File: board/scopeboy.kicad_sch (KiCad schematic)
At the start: 94 parts, among them J1 USB_C_Receptacle_USB2.0_16P, J2 SM03B-SRSS-TB, J3 SM03B-SRSS-TB, J4 Conn_01x10, J5 SM04B-SRSS-TB, J6 HDMI_A, SW1 SW_Push, SW2 SW_Push, SW3 RotaryEncoder_Switch, U1 W25Q128JVS, U2 DNF, U3 NCP1117-3.3_SOT223, U4 RP2350_80QFN, U5 LP2985-3.3, U6 LM27762, U7 ADC08060, Y1 ABM8-272-T3

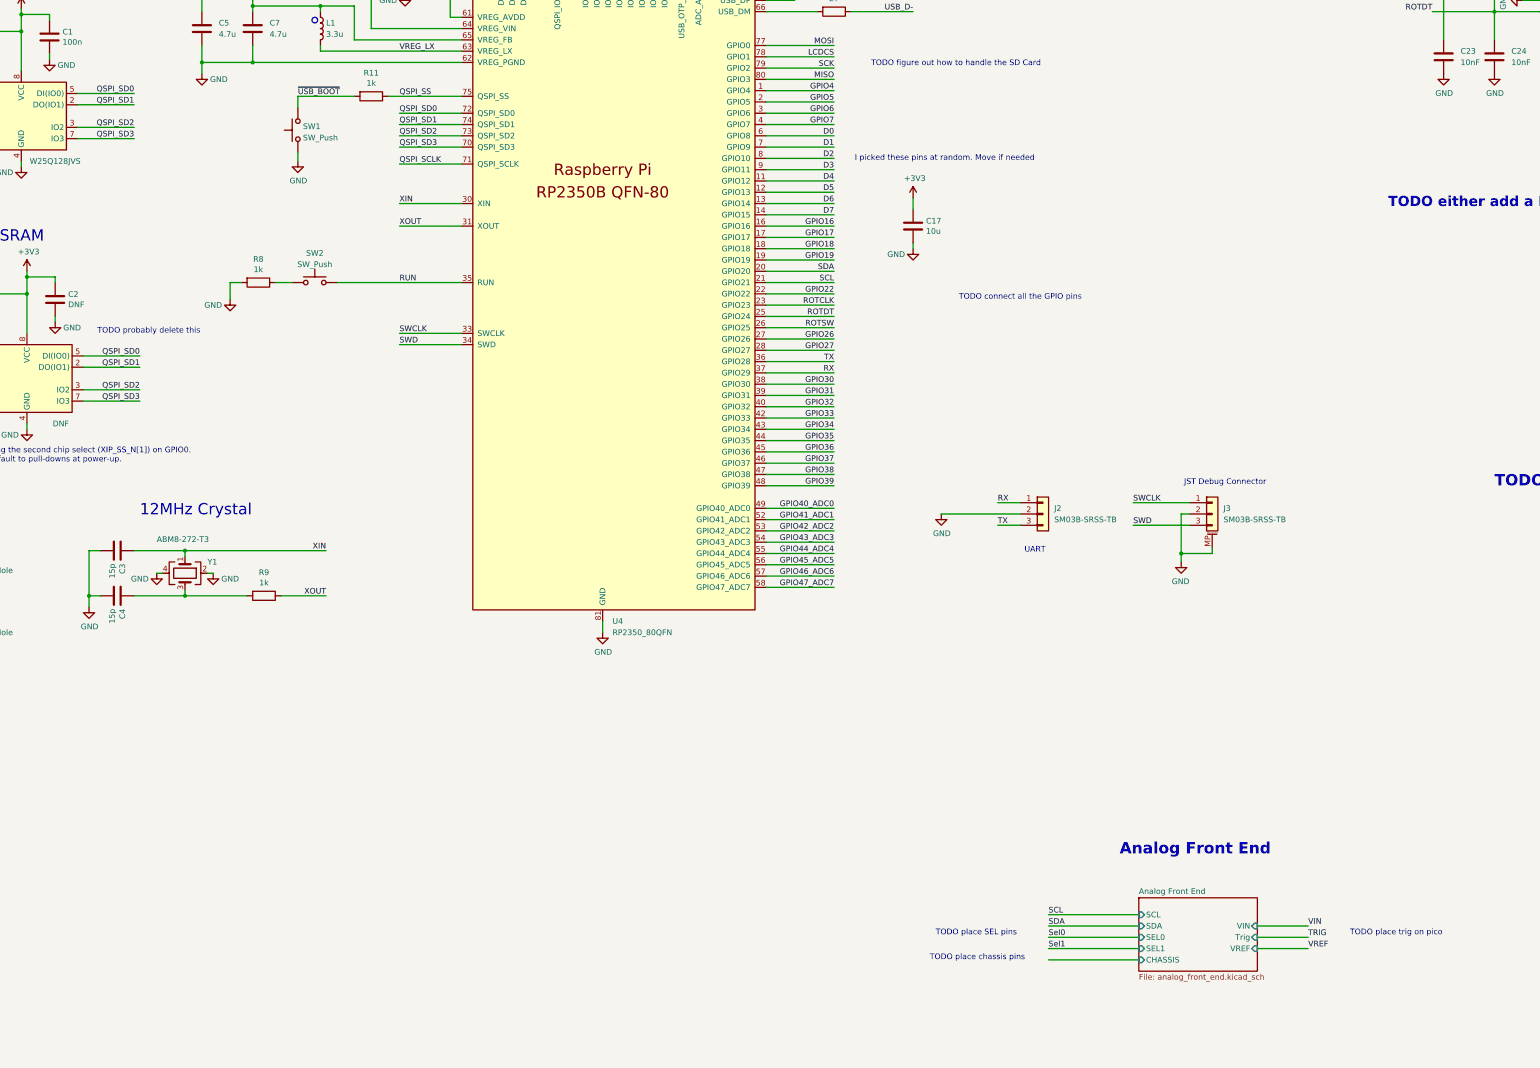
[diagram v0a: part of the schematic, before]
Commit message: Updated trig, sel0, sel1 pins
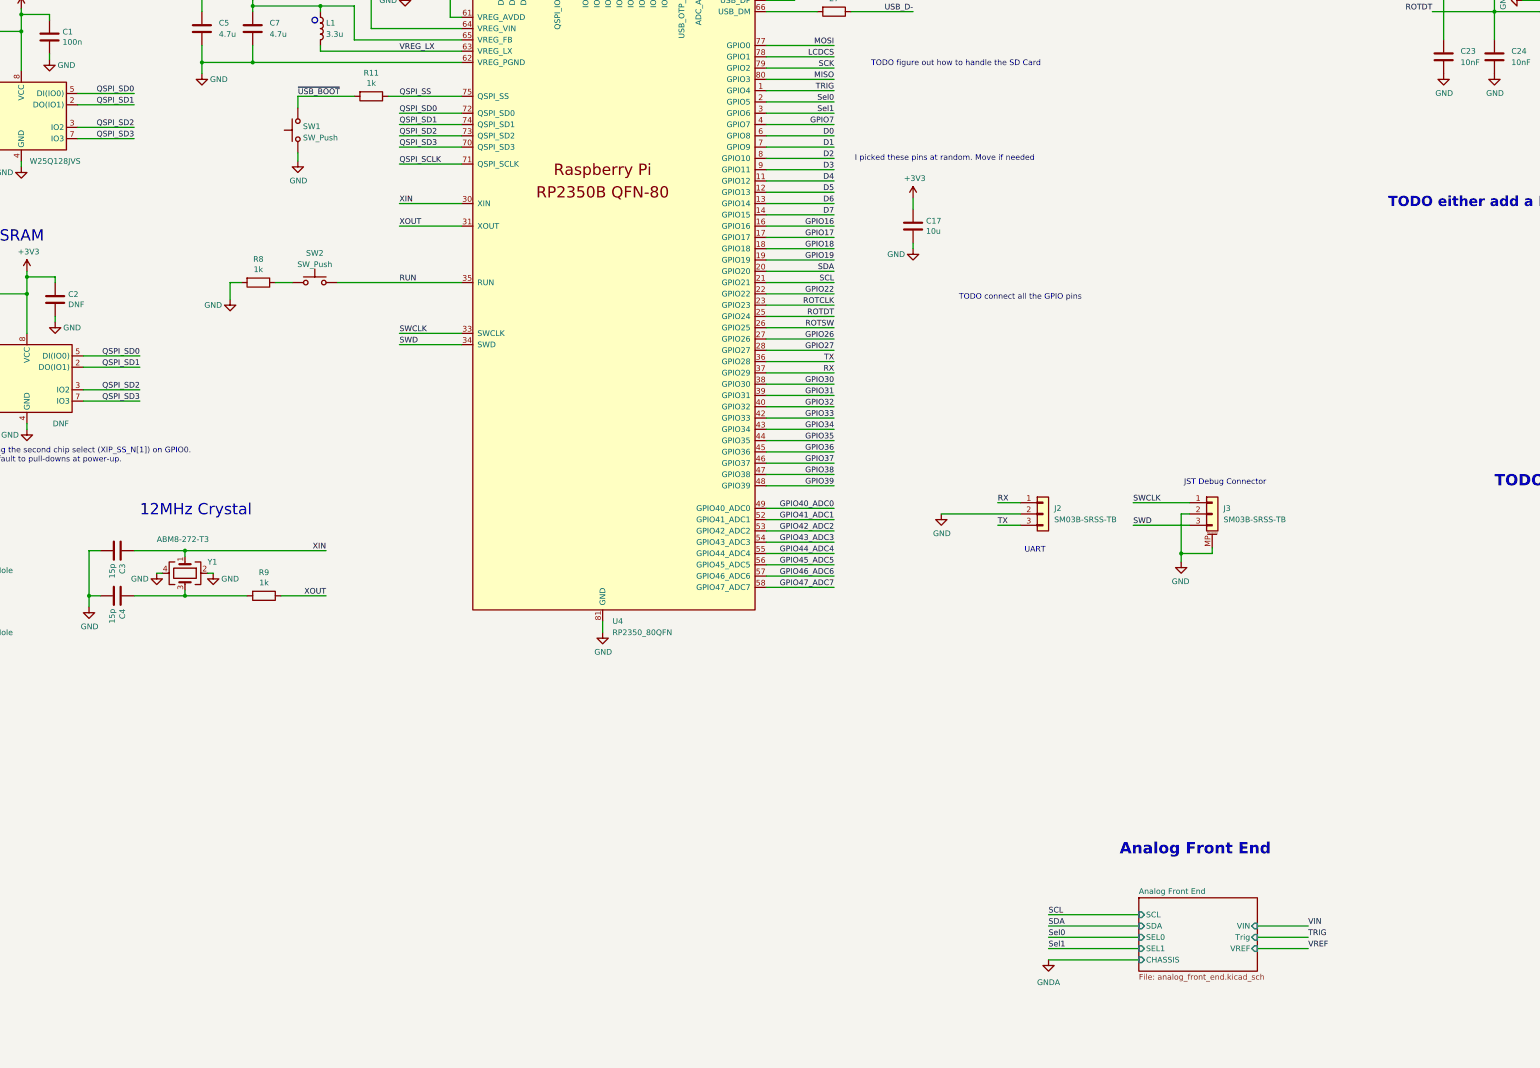
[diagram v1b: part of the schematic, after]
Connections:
- net GPIO4 is gone; now on net TRIG: U4.1 (GPIO4)
- net GPIO5 is gone; now on net Sel0: U4.2 (GPIO5)
- net GPIO6 is gone; now on net Sel1: U4.3 (GPIO6)
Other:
- note removed: "TODO place SEL pins"
- note removed: "TODO place chassis pins"
- note removed: "TODO place trig on pico"
- note removed: "TODO probably delete this"
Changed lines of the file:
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@@
 		)
 	)
-	(text "TODO place trig on pico"
-		(exclude_from_sim no)
-		(at 376.682 311.404 0)
-		(effects
-			(font
-				(size 1.27 1.27)
-			)
-		)
-	)
 	(text "12MHz Crystal"
 		(exclude_from_sim no)
@@
 		)
 	)
-	(text "TODO probably delete this"
-		(exclude_from_sim no)
-		(at 96.012 176.022 0)
-		(effects
-			(font
-				(size 1.27 1.27)
-			)
-		)
-	)
 	(text "Analog Front End"
 		(exclude_from_sim no)
@@
 		)
 	)
-	(text "TODO place SEL pins"
-		(exclude_from_sim no)
-		(at 282.194 311.404 0)
-		(effects
-			(font
-				(size 1.27 1.27)
-			)
-		)
-	)
 	(text "HDMI"
 		(exclude_from_sim no)
@@
 		)
 	)
-	(text "TODO place chassis pins"
-		(exclude_from_sim no)
-		(at 282.448 316.992 0)
-		(effects
-			(font
-				(size 1.27 1.27)
-			)
-		)
-	)
 	(junction
 		(at 52.07 60.96)
@@
 		)
 	)
+	(label "TRIG"
+		(at 250.19 121.92 180)
+		(effects
+			(font
+				(size 1.27 1.27)
+			)
+			(justify right bottom)
+		)
+	)
 	(label "SCL"
 		(at 250.19 165.1 180)
@@
 		)
 	)
+	(label "Sel0"
+		(at 250.19 124.46 180)
+		(effects
+			(font
+				(size 1.27 1.27)
+			)
+			(justify right bottom)
+		)
+	)
 	(label "SCK"
 		(at 250.19 116.84 180)
@@
 		)
 	)
+	(label "Sel1"
+		(at 250.19 127 180)
+		(effects
+			(font
+				(size 1.27 1.27)
+			)
+			(justify right bottom)
+		)
+	)
 	(label "GPIO36"
 		(at 250.19 203.2 180)
@@
 		)
 	)
-	(label "GPIO5"
-		(at 250.19 124.46 180)
-		(effects
-			(font
-				(size 1.27 1.27)
-			)
-			(justify right bottom)
-		)
-	)
 	(label "TX"
 		(at 287.02 219.71 0)
@@
 		)
 	)
-	(label "GPIO6"
-		(at 250.19 127 180)
-		(effects
-			(font
-				(size 1.27 1.27)
-			)
-			(justify right bottom)
-		)
-	)
 	(label "D1"
 		(at 250.19 134.62 180)
@@
 		)
 	)
-	(label "GPIO4"
-		(at 250.19 121.92 180)
-		(effects
-			(font
-				(size 1.27 1.27)
-			)
-			(justify right bottom)
-		)
-	)
 	(label "ROTSW"
 		(at 250.19 175.26 180)
@@
 					(unit 1)
 				)
+			)
+		)
+	)
+	(symbol
+		(lib_name "GNDA_1")
+		(lib_id "power:GNDA")
+		(at 298.45 317.5 0)
+		(unit 1)
+		(exclude_from_sim no)
+		(in_bom yes)
+		(on_board yes)
+		(dnp no)
+		(fields_autoplaced yes)
+		(property "Reference" "#PWR0143"
+			(at 298.45 323.85 0)
+			(effects
+				(font
+					(size 1.27 1.27)
+				)
+				(hide yes)
+			)
+		)
+		(property "Value" "GNDA"
+			(at 298.45 322.58 0)
+			(effects
+				(font
+					(size 1.27 1.27)
+				)
+			)
+		)
+		(property "Footprint" ""
+			(at 298.45 317.5 0)
+			(effects
+				(font
+					(size 1.27 1.27)
+				)
+				(hide yes)
+			)
+		)
+		(property "Datasheet" ""
+			(at 298.45 317.5 0)
+			(effects
+				(font
+					(size 1.27 1.27)
+				)
+				(hide yes)
+			)
+		)
+		(property "Description" "Power symbol creates a global label with name \"GNDA\" , analog ground"
+			(at 298.45 317.5 0)
+			(effects
+				(font
+					(size 1.27 1.27)
+				)
+				(hide yes)
+			)
+		)
+		(pin "1"
+		)
+		(instances
+			(project "scopeboy"
+				(path "/94683f5c-9cd9-448e-be96-9792537b5cb8"
+					(reference "#PWR0143")
+					(unit 1)
+				)

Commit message: Added battery JST connector
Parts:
- removed C29: 1u, Capacitor_SMD:C_0603_1608Metric, symbol Device:C
- removed C34: 10n, Capacitor_SMD:C_0603_1608Metric, symbol Device:C
- removed C37: 2.2u, Capacitor_SMD:C_0603_1608Metric, symbol Device:C
- removed U5: LP2985-3.3, Package_TO_SOT_SMD:SOT-23-5, symbol Regulator_Linear:LP2985-3.3
- added J8: Conn_01x02, Connector_JST:JST_PH_S2B-PH-SM4-TB_1x02-1MP_P2.00mm_Horizontal, symbol Connector_Generic:Conn_01x02
- U7: MFR. Part # (none) -> ADC08060CIMTX/NOPB; MRF. Part # ADC08060CIMTX/NOPB -> (none)
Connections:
- net VSYS is gone; now on net VBUS: C26.1, U6.12 (EN+), U6.3 (VIN), U6.8 (EN-)
- net GND: now also J8.2 (Pin_2)
- net VBUS: now also J8.1 (Pin_1)
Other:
- note added: "Battery Connector"
- note added: "TODO This should not connect directly to USB VBUS"
- note added: "TODO Update this to be a Buck Boost converter and add some way to handle both USB and Battery input"
- note removed: "PSU DIG."
- note removed: "TODO CHANGE THESE TO BATTERY VOLTAGES"
- note removed: "TODO either add a LiPo JST connector or a AA/AAA battery connector"
- note removed: "TODO this might need to be updated to work off of battery"
- note removed: "TODO this needs to be updated as well. I think I now have 2 digital power units with the analog side as well"

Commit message: Added power mux and USB protection
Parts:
- added C29: 10uF, Capacitor_SMD:C_1206_3216Metric, symbol Device:C
- added D6: SMBJ5.0A, Diode_SMD:D_SMB, symbol Device:D_Zener
- added F1: MINISMDC050F-2, Fuse:Fuse_1812_4532Metric, symbol Device:Polyfuse
- added R48: 100k, Resistor_SMD:R_0603_1608Metric, symbol Device:R
- added R49: 10K, Resistor_SMD:R_0603_1608Metric, symbol Device:R
- added R50: 47k, Resistor_SMD:R_0603_1608Metric, symbol Device:R
- added U5: TPS2116DRL, Package_TO_SOT_SMD:SOT-583-8, symbol Power_Management:TPS2116DRL
- R6, R7: MFR. Part # (none) -> CRCW12065K10FKEA; Manufacturer Part Number CRCW12065K10FKEA -> (none)
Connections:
- net GPIO32 is gone; now on net D0: U4.40 (GPIO32)
- net GPIO33 is gone; now on net D1: U4.42 (GPIO33)
- net GPIO34 is gone; now on net D2: U4.43 (GPIO34)
- net GPIO35 is gone; now on net D3: U4.44 (GPIO35)
- net GPIO36 is gone; now on net D4: U4.45 (GPIO36)
- net GPIO37 is gone; now on net D5: U4.46 (GPIO37)
- net GPIO38 is gone; now on net D6: U4.47 (GPIO38)
- net GPIO39 is gone; now on net D7: U4.48 (GPIO39)
- net +5V: no longer J6.18 (+5V), R19.1, R19.2
- net D0: no longer U4.6 (GPIO8)
- net D1: no longer U4.7 (GPIO9)
- net D2: no longer U4.8 (GPIO10)
- net D3: no longer U4.9 (GPIO11)
- net D4: no longer U4.11 (GPIO12)
- net D5: no longer U4.12 (GPIO13)
- net D6: no longer U4.13 (GPIO14)
- net D7: no longer U4.14 (GPIO15)
- net GND: now also J1.S1 (SHIELD), C29.1, D6.2 (A), R50.2, U5.1 (GND)
- net VBUS: now also J6.18 (+5V), R19.1, R19.2, C29.2, D6.1 (K), F1.2, R48.1, U5.3 (VIN1), U5.5 (MODE); no longer C6.1, J1.A4 (VBUS), J1.A9 (VBUS), J1.B4 (VBUS), J1.B9 (VBUS), J8.1 (Pin_1), U3.3 (VI)
- net GPIO12 renamed HDMI_D2P
- net HDMI_D2P: now also U4.11 (GPIO12)
- net GPIO13 renamed HDMI_D2N
- net HDMI_D2N: now also U4.12 (GPIO13)
- net GPIO14 renamed HDMI_CKP
- net HDMI_CKP: now also U4.13 (GPIO14)
- net GPIO15 renamed HDMI_CKN
- net HDMI_CKN: now also U4.14 (GPIO15)
- net GPIO16 renamed HDMI_D1P
- net GPIO17 renamed HDMI_D1N
- net GPIO18 renamed HDMI_D0P
- net GPIO19 renamed HDMI_D0N
- net GPIO7 renamed PowerStatus
- net PowerStatus: now also R49.1, U5.8 (ST)
- new net: F1.1, J1.A4 (VBUS), J1.A9 (VBUS), J1.B4 (VBUS), J1.B9 (VBUS)
- new net: R48.2, R50.1, U5.4 (PR1)
- new net VBat: J8.1 (Pin_1), U5.6 (VIN2)
- new net VDC: C6.1, R49.2, U3.3 (VI), U5.2 (VOUT), U5.7 (VOUT)
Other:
- note added: "HDMI use HSTX pins, they cannot be moved"
- note added: "I picked these pins (mostly) at random. Move if needed"
- note added: "Power Mux"
- note added: "TODO SD card should probably be on these pins since they are all SPI1"
- note added: "TODO Update this to be a Buck Boost converter"
- note added: "USB Protection"
- note added: "VBus is USB"
- note removed: "I picked these pins at random. Move if needed"
- note removed: "TODO This should not connect directly to USB VBUS"
- note removed: "TODO Update this to be a Buck Boost converter and add some way to handle both USB and Battery input"
- note removed: "TODO figure out how to handle the SD Card"
- moved on the sheet: C17, C6, C9, J8, U3

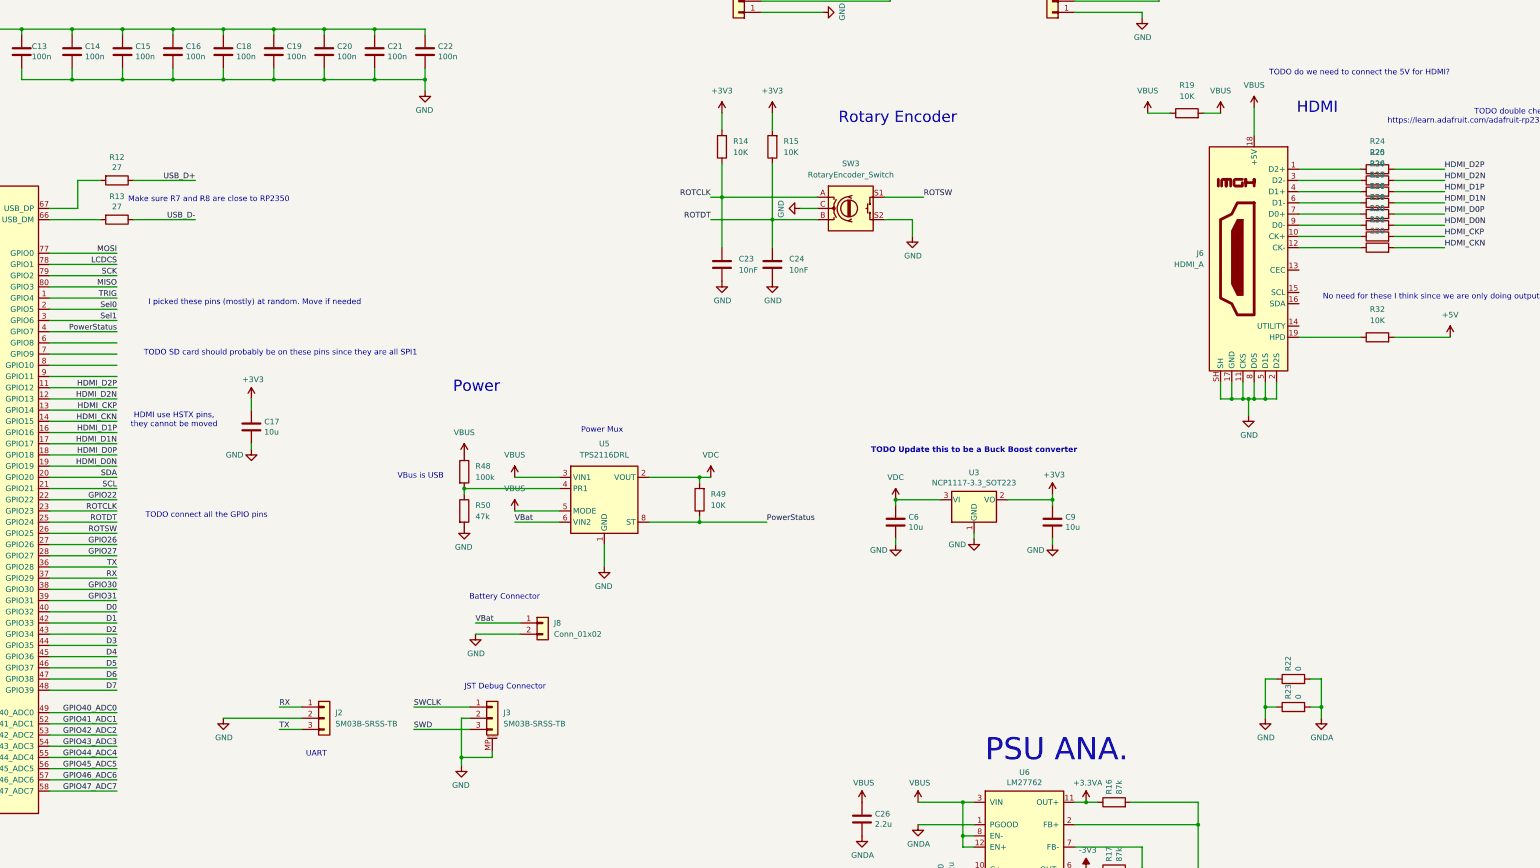
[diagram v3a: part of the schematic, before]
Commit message: Updated board with new power system
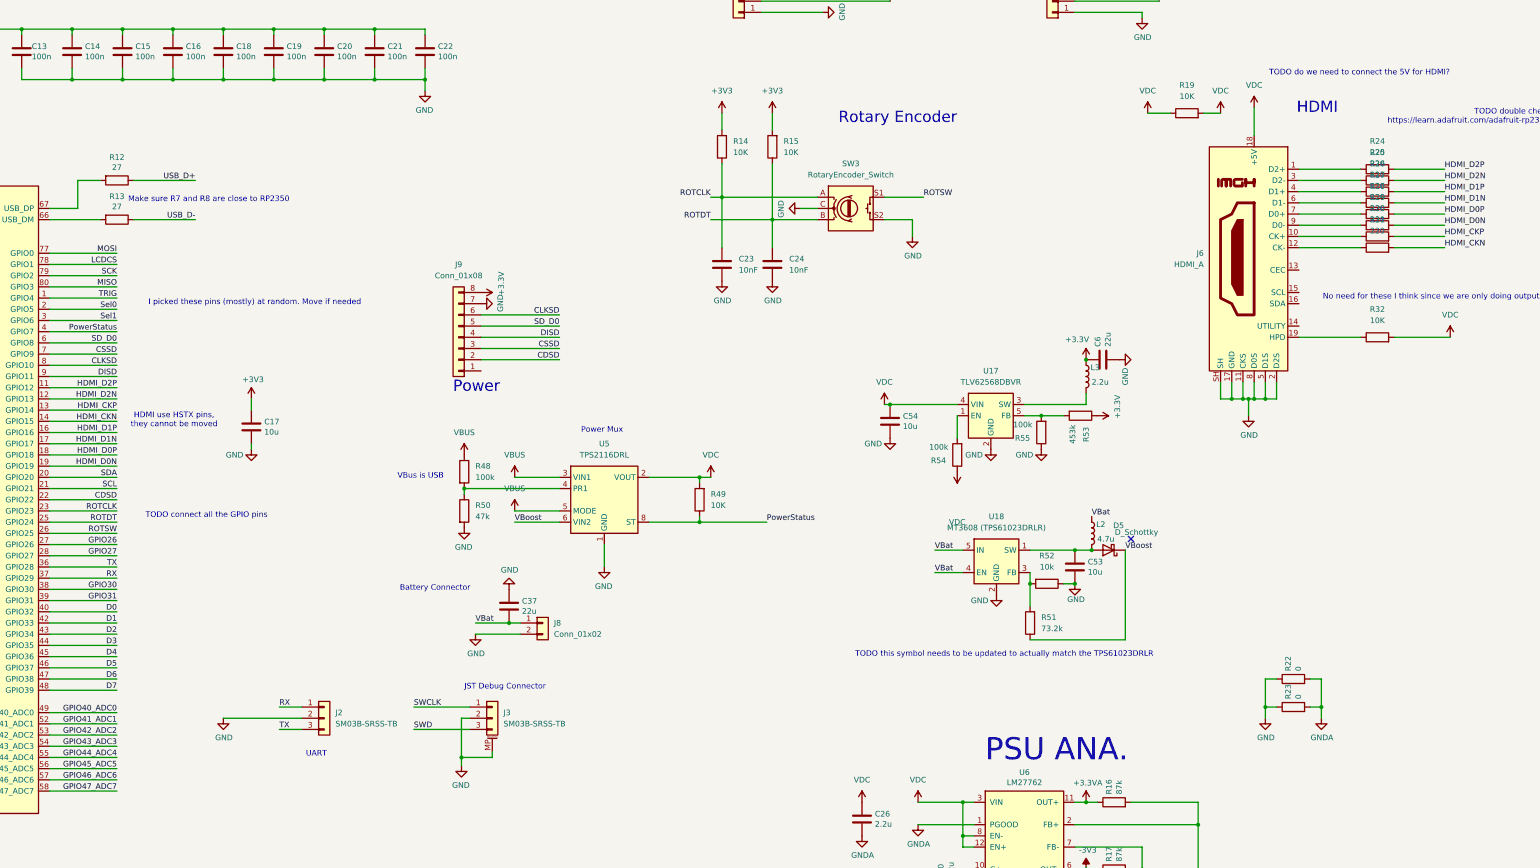
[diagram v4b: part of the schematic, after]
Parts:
- removed C9: 10u, Capacitor_SMD:C_0805_2012Metric, symbol Device:C
- removed U3: NCP1117-3.3_SOT223, Package_TO_SOT_SMD:SOT-223-3_TabPin2, symbol Regulator_Linear:NCP1117-3.3_SOT223
- added C37: 22u, Capacitor_SMD:C_0805_2012Metric, symbol Device:C
- added C53, C54: 10u, Capacitor_SMD:C_0805_2012Metric, symbol Device:C
- added D5: D_Schottky, Diode_SMD:D_SMA, symbol Device:D_Schottky
- added J9: Conn_01x08, Connector_PinHeader_2.54mm:PinHeader_1x08_P2.54mm_Vertical, symbol Connector_Generic:Conn_01x08
- added L2: 4.7u, Inductor_SMD:L_Bourns-SRN4018, symbol Device:L
- added L3: 2.2u, Inductor_SMD:L_Bourns-SRN4018, symbol Device:L
- added R51: 73.2k, Resistor_SMD:R_0603_1608Metric, symbol Device:R
- added R52: 10k, Resistor_SMD:R_0603_1608Metric, symbol Device:R
- added R53: 453k, Resistor_SMD:R_0603_1608Metric, symbol Device:R
- added R54, R55: 100k, Resistor_SMD:R_0603_1608Metric, symbol Device:R
- added U17: TLV62568DBVR, Package_TO_SOT_SMD:SOT-23-5, symbol Regulator_Switching:TLV62568DBV
- added U18: MT3608 (TPS61023DRLR), Package_TO_SOT_SMD:SOT-23-6, symbol Regulator_Switching:MT3608
- C6: value 10u -> 22u
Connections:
- net +5V is gone; now on net VDC: R32.2
- net GND: now also C37.1, C53.2, C54.2, J9.7 (Pin_7), R52.1, R55.1, U17.2 (GND), U18.2 (GND)
- net VBUS: no longer C26.1, J6.18 (+5V), R19.1, R19.2, U6.12 (EN+), U6.3 (VIN), U6.8 (EN-)
- net VBat: now also C37.2, L2.1, U18.4 (EN), U18.5 (IN); no longer U5.6 (VIN2)
- net VDC: now also C26.1, J6.18 (+5V), R19.1, R19.2, U6.12 (EN+), U6.3 (VIN), U6.8 (EN-), C54.1, R54.1, U17.4 (VIN); no longer C6.1
- net SD_D0: now reaches U4.6 (GPIO8)
- net SD_D0: now also J9.5 (Pin_5)
- net CSSD: now reaches U4.7 (GPIO9)
- net CSSD: now also J9.3 (Pin_3)
- net CLKSD: now reaches U4.8 (GPIO10)
- net CLKSD: now also J9.6 (Pin_6)
- net DISD: now reaches U4.9 (GPIO11)
- net DISD: now also J9.4 (Pin_4)
- net GPIO22 renamed CDSD
- net CDSD: now also J9.2 (Pin_2)
- new net: C53.1, D5.2 (A), L2.2, U18.1 (SW)
- new net: R54.2, U17.1 (EN)
- new net: R53.2, R55.2, U17.5 (FB)
- new net: L3.2, U17.3 (SW)
- new net: R51.2, R52.2, U18.3 (FB)
- new net +3.3V: C6.1, J9.8 (Pin_8), L3.1, R53.1
- new net VBoost: D5.1 (K), R51.1, U5.6 (VIN2)
- no-connect marks 0 -> 1
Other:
- note added: "TODO this symbol needs to be updated to actually match the TPS61023DRLR"
- note removed: "TODO SD card should probably be on these pins since they are all SPI1"
- note removed: "TODO Update this to be a Buck Boost converter"
